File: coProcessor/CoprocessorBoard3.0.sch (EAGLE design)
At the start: 87 parts, among them IC1 STM32F405RGT6, J1 5008730806

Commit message: Mega cleanup and initial placement of rev3 parts
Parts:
- removed D+PULL, D-PULL: 1.5k, SparkFun-Resistors:1KOHM-HORIZ-1/4W-1%
- removed DEPTH_SENSOR: NANOFIT4PIN, nanofit 4pin:NANOFIT4PIN
- removed ESC_CONNECTOR_1, ESC_CONNECTOR_3: 455-1750-1-ND, SparkFun-Connectors:CONN_03
- removed J1: 5008730806, 5008730806:5008730806
- removed OPTOCOUPLER_1, OPTOCOUPLER_3: SFH610, optocoupler:SFH610
- removed O_IN_1, O_IN_3: 220, SparkFun-Resistors:1KOHM-HORIZ-1/4W-1%
- removed O_R1, O_R3: 10k, SparkFun-Resistors:1KOHM-HORIZ-1/4W-1%
- added U$2: NANOFIT_4PIN_STR, nanofit_4pin_str:NANOFIT_4PIN_STR
- CPC1: value 100nF -> 0.1uF
- CPC3: device SparkFun-Capacitors:4.7UF-1206-16V-(+80/-20%) -> SparkFun-Capacitors:4.7UF0603
- CPC5, CPC6, CPC7, CPC8: value 1nF -> 0.1uF
- renumbered 5V_LED1 to 3V_LED, 5V_R1 to 3V_R
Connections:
- removed net +3.3V: D+PULL.2, D-PULL.2, DEPTH_SENSOR.CKT_1, J1.VCC, JTAG_CONNECTOR.1, JTAG_CONNECTOR.2, POWER_JACK.1, R_DS_1.2, R_DS_2.2, SWITCH_CONNECTOR.CK10, SWITCH_CONNECTOR.CK11, SWITCH_CONNECTOR.CK12, SWITCH_CONNECTOR.CK7, SWITCH_CONNECTOR.CK8, SWITCH_CONNECTOR.CK9, U$1.3.3V_1, U$1.3.3V_2, U$1.3.3V_3, U$1.3.3V_4, U$1.3.3V_5, U$1.3.3V_6
- removed net GND1: 5V_LED.C
- removed net GNDA: U$1.EXTRA24, VOLTAGE_REGULATOR.GND
- removed net GND_THRUSTER: ESC_CONNECTOR_1.3, ESC_CONNECTOR_10.3, ESC_CONNECTOR_2.3, ESC_CONNECTOR_3.3, ESC_CONNECTOR_4.3, ESC_CONNECTOR_5.3, ESC_CONNECTOR_6.3, ESC_CONNECTOR_7.3, ESC_CONNECTOR_8.3, ESC_CONNECTOR_9.3, O_R1.2, O_R10.2, O_R2.2, O_R3.2, O_R4.2, O_R5.2, O_R6.2, O_R7.2, O_R8.2, O_R9.2
- removed net N$1: ESC_CONNECTOR_1.1, OPTOCOUPLER_1.EMIT, O_R1.1
- removed net N$20: OPTOCOUPLER_3.A, O_IN_3.2
- removed net N$22: OPTOCOUPLER_1.A, O_IN_1.2
- removed net N$35: CAP1.1, CAP2.1, IC1.VCAP_1, IC1.VCAP_2
- removed net N$5: ESC_CONNECTOR_3.1, OPTOCOUPLER_3.EMIT, O_R3.1
- removed net V+: 3V_R.1, CPC1.1, CPC2.1, CPC3.1, CPC5.1, CPC6.1, CPC7.1, CPC8.1, IC1.VDD(1), IC1.VDD(2), IC1.VDD(3), IC1.VDD(4), IC1.VDDA
- new net 3V3: 3V_R.1, CPC1.1, CPC2.1, CPC3.1, CPC5.1, CPC6.1, CPC7.1, CPC8.1, IC1.VDD(1), IC1.VDD(2), IC1.VDD(3), IC1.VDD(4), IC1.VDDA, JTAG_CONNECTOR.1, JTAG_CONNECTOR.2, POWER_JACK.1, R_DS_1.2, R_DS_2.2, SWITCH_CONNECTOR.CK10, SWITCH_CONNECTOR.CK11, SWITCH_CONNECTOR.CK12, SWITCH_CONNECTOR.CK7, SWITCH_CONNECTOR.CK8, SWITCH_CONNECTOR.CK9, U$1.3.3V_1, U$1.3.3V_2, U$1.3.3V_3, U$1.3.3V_4, U$1.3.3V_5, U$1.3.3V_6, U$2.P$1
- new net GNDBAT: 5V_LED.C, ESC_CONNECTOR_10.3, ESC_CONNECTOR_2.3, ESC_CONNECTOR_4.3, ESC_CONNECTOR_5.3, ESC_CONNECTOR_6.3, ESC_CONNECTOR_7.3, ESC_CONNECTOR_8.3, ESC_CONNECTOR_9.3, O_R10.2, O_R2.2, O_R4.2, O_R5.2, O_R6.2, O_R7.2, O_R8.2, O_R9.2, U$1.EXTRA24, VOLTAGE_REGULATOR.GND
- new net KILL_SWITCH: IC1.PC15, U$1.KILL_SWITCH
- new net VCAP1: CAP1.1, IC1.VCAP_1
- new net VCAP2: CAP2.1, IC1.VCAP_2
- net +5V: no longer OPTOCOUPLER_1.COL, OPTOCOUPLER_3.COL
- net D+CON: no longer D+PULL.1
- net D-CON: no longer D-PULL.1
- net DEPTHSCL: now also U$2.P$3; no longer DEPTH_SENSOR.CKT_2
- net DEPTHSDA: now also U$2.P$2; no longer DEPTH_SENSOR.CKT_3
- net GND: now also U$2.P$4; no longer DEPTH_SENSOR.CKT_4, J1.GND, J1.SHIELD, OPTOCOUPLER_1.C, OPTOCOUPLER_3.C
- net SDIO_CK: no longer J1.CLK(SCK)
- net SDIO_CMD: no longer J1.CMD(DI)
- net SDIO_DO: no longer J1.DAT0(DO)
- net SURGEPORTHI: no longer O_IN_3.1
- net SURGESTBDHI: no longer O_IN_1.1
- net SWITCH_3: now also SWITCH_CONNECTOR.CK5; no longer SWITCH_CONNECTOR.CK3
- net SWITCH_5: now also SWITCH_CONNECTOR.CK3; no longer SWITCH_CONNECTOR.CK5
- net USB_OTG_HS_DM: now also IC1.PB14
- net USB_OTG_HS_DP: now also IC1.PB15
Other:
- moved on the sheet: R_DS_1

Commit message: Final-ish placement of parts
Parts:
- removed S1: TL42YO, switch:TL42YO
- added SW1: (no value), special:SW_DIP-4
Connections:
- net JTAG_5: now also SW1.5, SW1.7; no longer S1.O, S1.O1
- net JTAG_7: now also SW1.6, SW1.8; no longer S1.S, S1.S1
- net SYS_JTDI: now also SW1.3, SW1.4; no longer S1.P
- net SYS_JTMS-SWIDIO: now also SW1.1, SW1.2; no longer S1.P1

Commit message: (Hulk) Smash
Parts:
- added C1: (no value), rcl:CPOL-USE2-5
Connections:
- net 3V3: now also C1.+
- net GND: now also C1.-
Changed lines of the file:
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@@
 <part name="U$2" library="nanofit_4pin_str" deviceset="NANOFIT_4PIN_STR" device=""/>
 <part name="SW1" library="special" library_urn="urn:adsk.eagle:library:367" deviceset="SW_DIP-4" device="" package3d_urn="urn:adsk.eagle:package:26655/2"/>
+<part name="C1" library="rcl" library_urn="urn:adsk.eagle:library:334" deviceset="CPOL-US" device="E2-5" package3d_urn="urn:adsk.eagle:package:23346/2"/>
 </parts>
 <sheets>
@@
 <attribute name="NAME" x="-25.3941" y="252.72488125" size="1.27073125" layer="95" rot="R180"/>
 </instance>
-<instance part="3.3V" gate="1" x="-167.64" y="119.38" rot="R270"/>
-<instance part="GND1" gate="1" x="-167.64" y="132.08"/>
+<instance part="3.3V" gate="1" x="-149.86" y="119.38" rot="R270"/>
+<instance part="GND1" gate="1" x="-152.4" y="132.08"/>
 <instance part="P+1" gate="1" x="-170.18" y="200.66" smashed="yes" rot="R270">
 <attribute name="VALUE" x="-165.1" y="200.66" size="1.778" layer="96"/>
@@
 <instance part="U$2" gate="G$1" x="-76.2" y="233.68"/>
 <instance part="SW1" gate="A" x="-58.42" y="210.82" rot="MR90"/>
+<instance part="C1" gate="G$1" x="-165.1" y="127" rot="R180"/>
 </instances>
 <busses>
@@
 <junction x="-175.26" y="119.38"/>
 <pinref part="3.3V" gate="1" pin="V+"/>
-<wire x1="-175.26" y1="119.38" x2="-170.18" y2="119.38" width="0.1524" layer="91"/>
+<wire x1="-175.26" y1="119.38" x2="-165.1" y2="119.38" width="0.1524" layer="91"/>
+<pinref part="C1" gate="G$1" pin="+"/>
+<wire x1="-165.1" y1="119.38" x2="-152.4" y2="119.38" width="0.1524" layer="91"/>
+<wire x1="-165.1" y1="124.46" x2="-165.1" y2="119.38" width="0.1524" layer="91"/>
+<junction x="-165.1" y="119.38"/>
 </segment>
 <segment>
@@
 <junction x="-175.26" y="134.62"/>
 <pinref part="GND1" gate="1" pin="GND"/>
-<wire x1="-175.26" y1="134.62" x2="-167.64" y2="134.62" width="0.1524" layer="91"/>
-</segment>
-<segment>
+<wire x1="-175.26" y1="134.62" x2="-165.1" y2="134.62" width="0.1524" layer="91"/>
+<pinref part="C1" gate="G$1" pin="-"/>
+<wire x1="-165.1" y1="134.62" x2="-152.4" y2="134.62" width="0.1524" layer="91"/>
+<wire x1="-165.1" y1="132.08" x2="-165.1" y2="134.62" width="0.1524" layer="91"/>
+<junction x="-165.1" y="134.62"/>
+</segment>
+<segment>

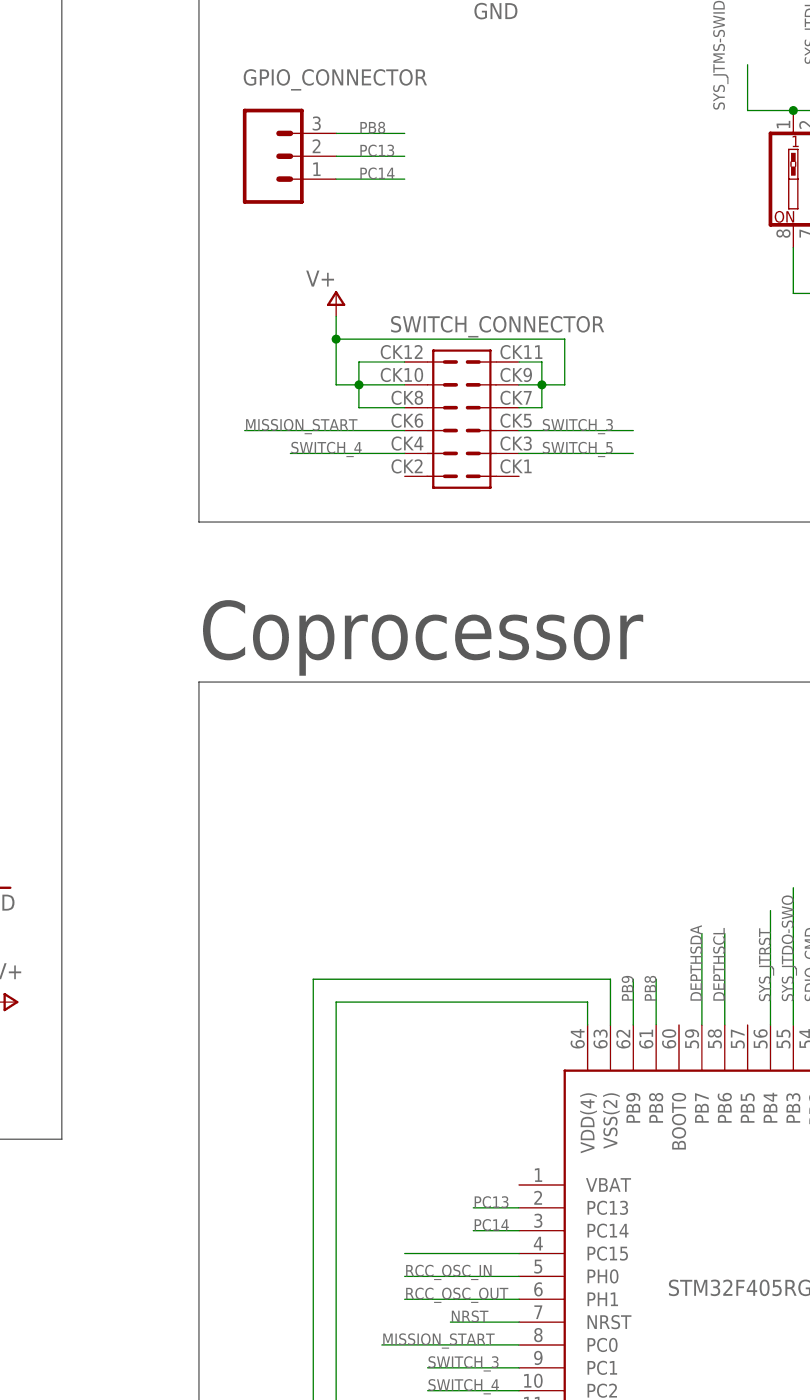
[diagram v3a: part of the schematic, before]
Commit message: Adding labels to everything
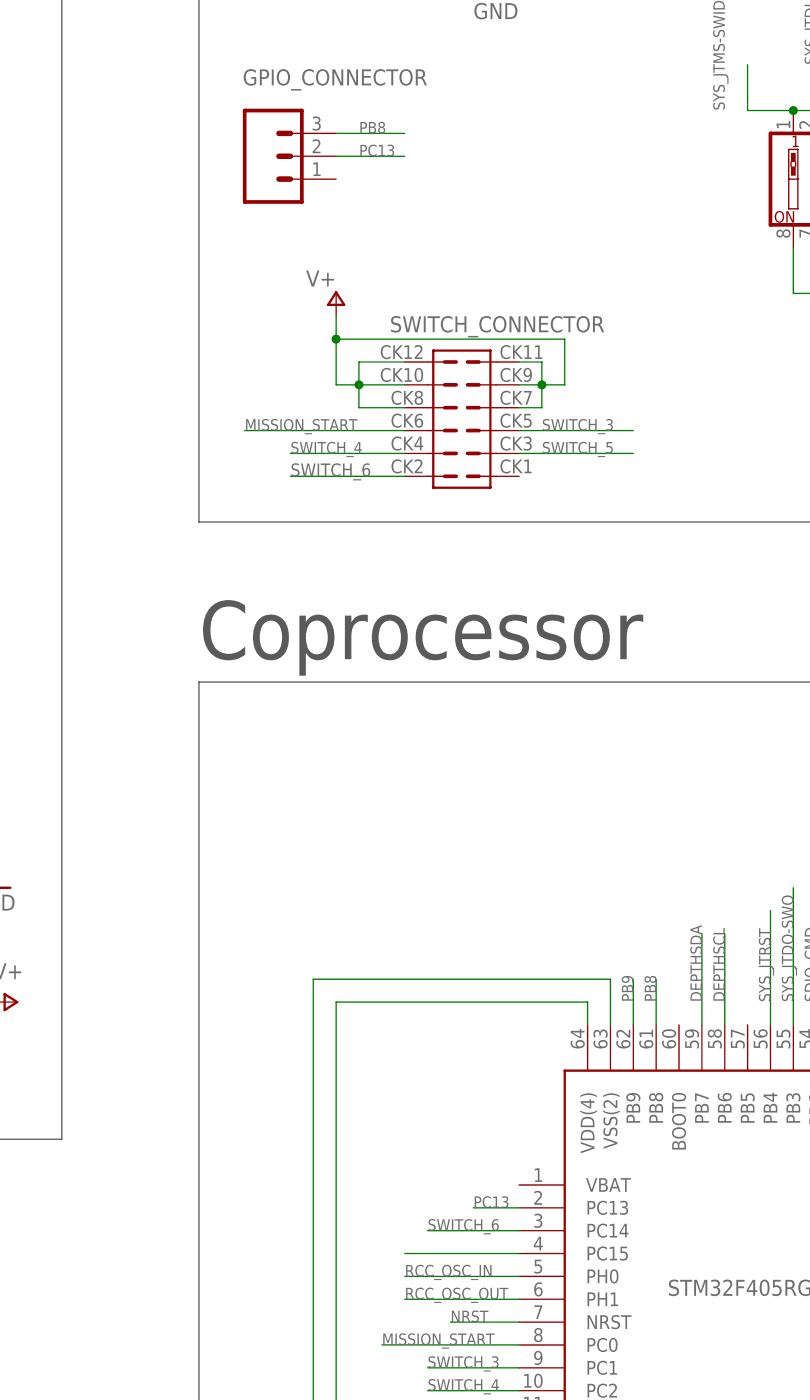
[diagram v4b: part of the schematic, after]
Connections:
- removed net PC14: GPIO_CONNECTOR.1, IC1.PC14
- new net SWITCH_6: IC1.PC14, SWITCH_CONNECTOR.CK2
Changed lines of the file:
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@@
-</segment>
-</net>
-<net name="PC14" class="0">
-<segment>
-<pinref part="GPIO_CONNECTOR" gate="J$1" pin="1"/>
-<wire x1="-114.3" y1="210.82" x2="-106.68" y2="210.82" width="0.1524" layer="91"/>
-<label x="-111.76" y="210.82" size="1.27" layer="95"/>
-</segment>
-<segment>
-<pinref part="IC1" gate="G$1" pin="PC14"/>
-<wire x1="-93.98" y1="93.98" x2="-99.06" y2="93.98" width="0.1524" layer="91"/>
-<label x="-99.06" y="93.98" size="1.27" layer="95"/>
 </segment>
 </net>
@@
 </segment>
 </net>
+<net name="SWITCH_6" class="0">
+<segment>
+<pinref part="SWITCH_CONNECTOR" gate="G$1" pin="CK2"/>
+<wire x1="-106.68" y1="177.8" x2="-119.38" y2="177.8" width="0.1524" layer="91"/>
+<label x="-119.38" y="177.8" size="1.4224" layer="95"/>
+</segment>
+<segment>
+<pinref part="IC1" gate="G$1" pin="PC14"/>
+<label x="-104.14" y="93.98" size="1.27" layer="95"/>
+<wire x1="-93.98" y1="93.98" x2="-104.14" y2="93.98" width="0.1524" layer="91"/>
+</segment>
+</net>

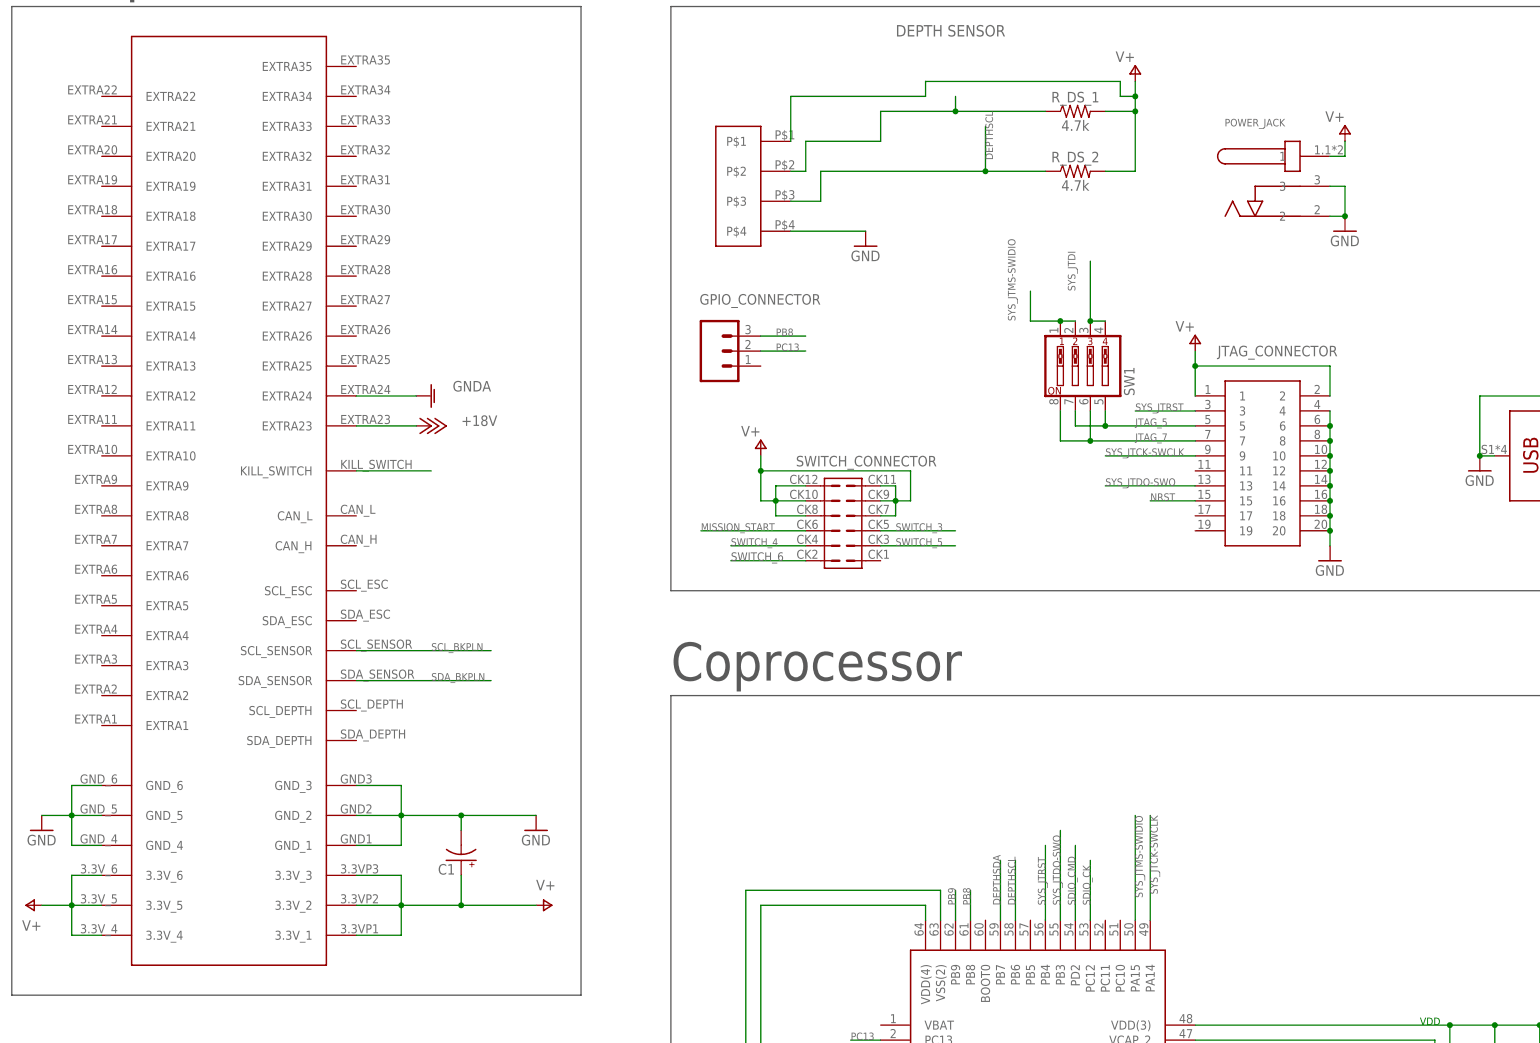
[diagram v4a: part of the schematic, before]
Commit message: Added low pass filter, ran DRC fixed weird issue
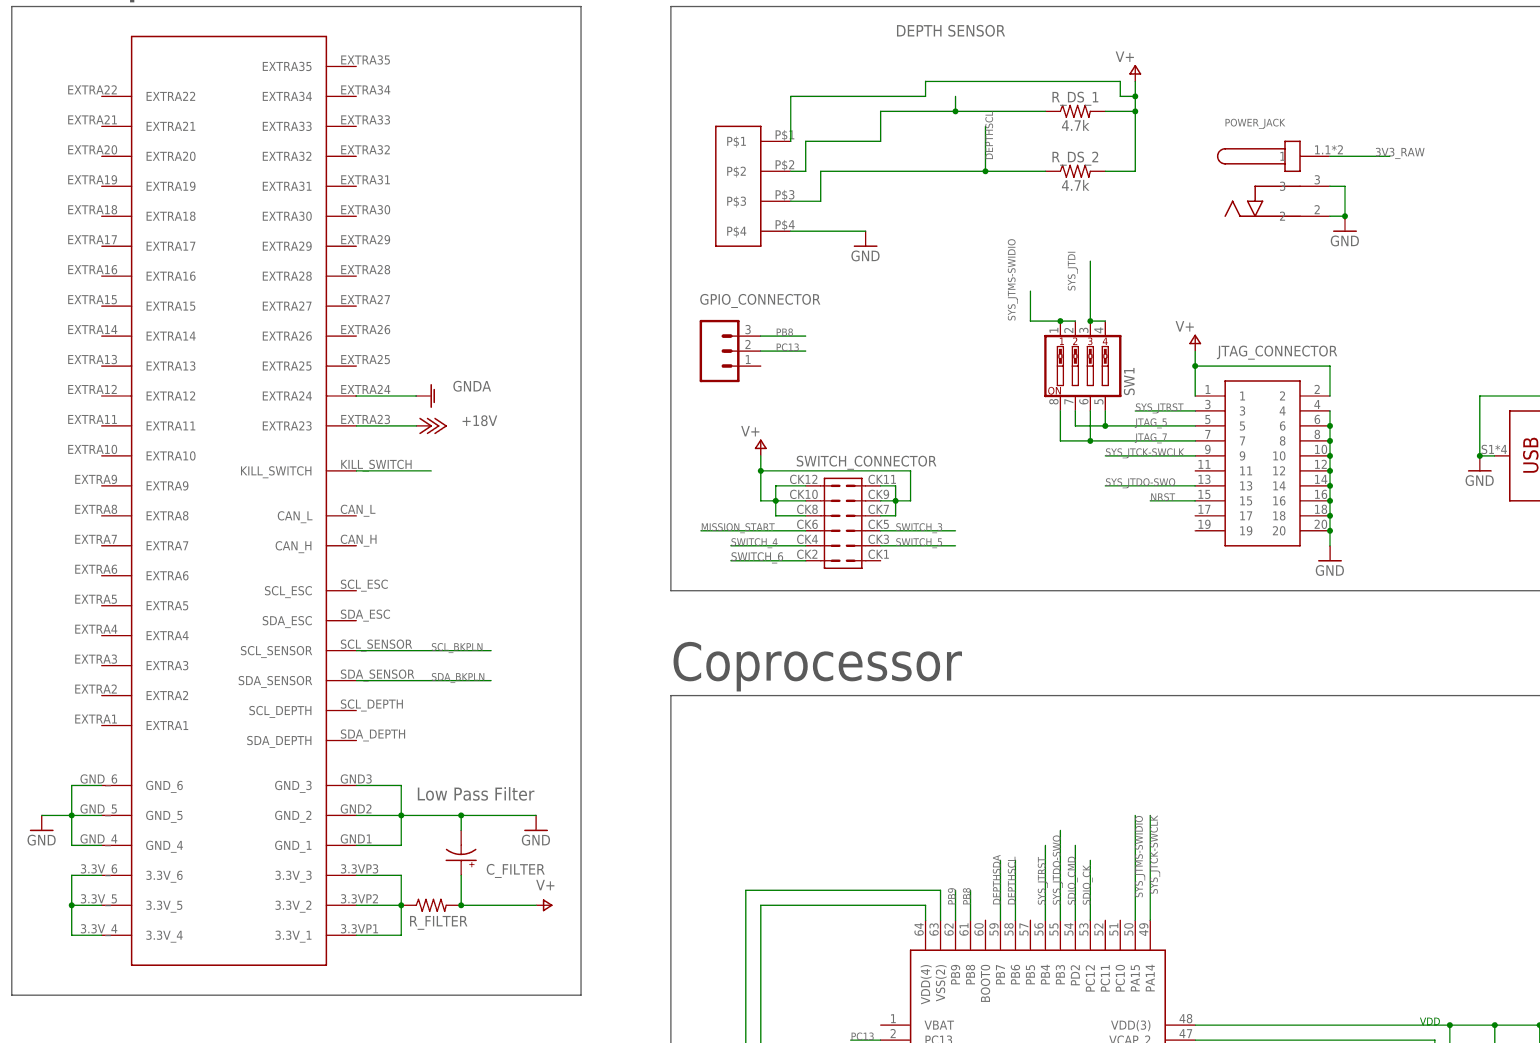
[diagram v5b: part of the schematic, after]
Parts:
- added R_FILTER: (no value), rcl:R-US_0204/7
- renumbered C1 to C_FILTER
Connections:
- new net 3V3_RAW: POWER_JACK.1, R_FILTER.1, U$1.3.3V_1, U$1.3.3V_2, U$1.3.3V_3, U$1.3.3V_4, U$1.3.3V_5, U$1.3.3V_6
- net 3V3: now also R_FILTER.2; no longer POWER_JACK.1, U$1.3.3V_1, U$1.3.3V_2, U$1.3.3V_3, U$1.3.3V_4, U$1.3.3V_5, U$1.3.3V_6
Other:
- note added: "Low Pass Filter"

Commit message: Merging to fix with the stuff
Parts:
- added ESC_CONNECTOR_1: 455-1750-1-ND, SparkFun-Connectors:CONN_03
- added OPTOCOUPLER_1: SFH610, optocoupler:SFH610
- added O_IN_1: 220, SparkFun-Resistors:1KOHM-HORIZ-1/4W-1%
- added O_R1: 10k, SparkFun-Resistors:1KOHM-HORIZ-1/4W-1%
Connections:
- new net N$1: ESC_CONNECTOR_1.1, OPTOCOUPLER_1.EMIT, O_R1.1
- new net N$3: OPTOCOUPLER_1.A, O_IN_1.2
- net +5V: now also OPTOCOUPLER_1.COL
- net GND: now also OPTOCOUPLER_1.C
- net GNDBAT: now also ESC_CONNECTOR_1.3, O_R1.2
- net SURGEPORTHI: now also O_IN_1.1
